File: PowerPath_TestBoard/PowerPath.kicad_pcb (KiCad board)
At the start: 2 copper layers, 105.4 x 62.9 mm, 102 parts, among them IC1 LM74502DDFR, J1 24V Test, J2 +24V_Ext, J3 12V Test, J4 5V Test, J5 3V Test, J6 +V_in_24V, J7 GND, J8 +Vin_5V, Q1 PSMN012-100YS, Q2 PSMN012-100YS, U1 MCP1826S_LDO, U2 LMR51635XDDCR, U3 LMR51635XDDCR

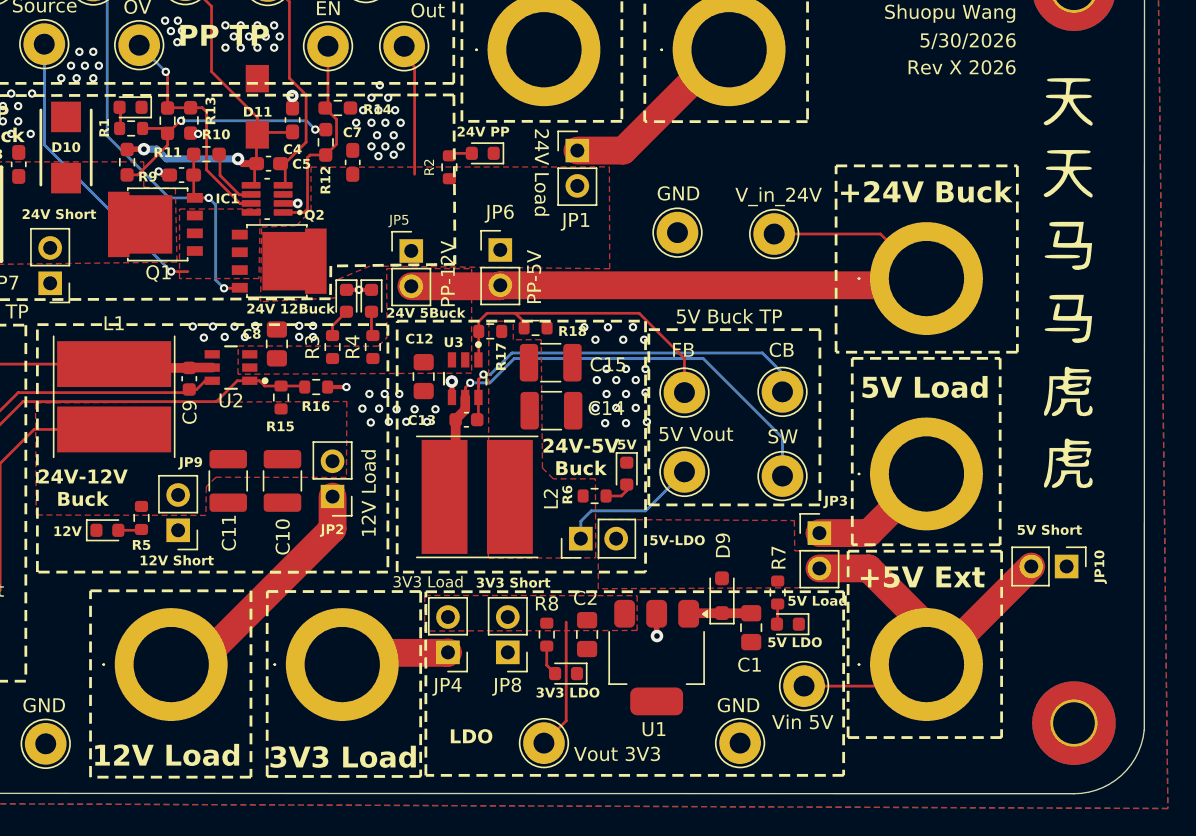
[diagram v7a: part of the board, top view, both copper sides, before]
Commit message: updated with new comments + new gen gebers
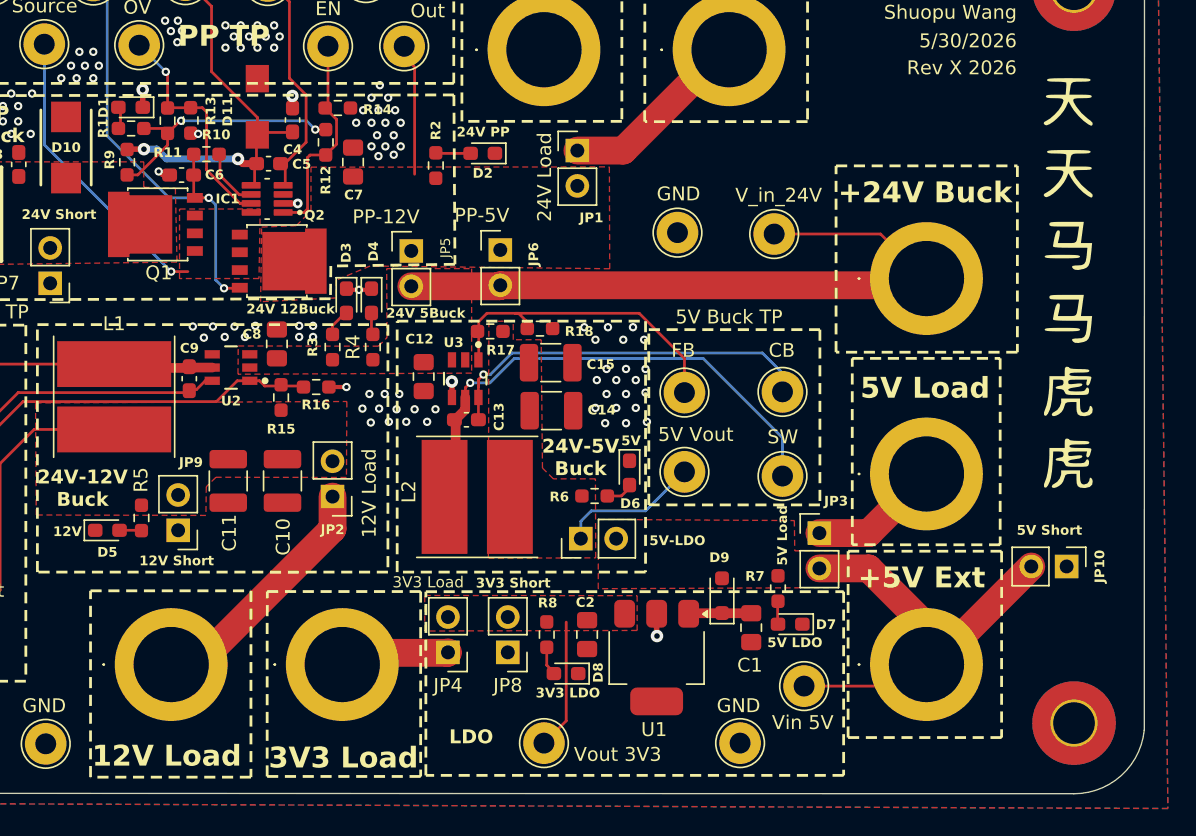
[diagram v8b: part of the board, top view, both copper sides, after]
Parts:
- C13, C9: footprint Capacitor_SMD:C_0603_1608Metric -> Capacitor_SMD:C_0603_1608Metric_Pad1.08x0.95mm_HandSolder
- C7: footprint Capacitor_SMD:C_0603_1608Metric_Pad1.08x0.95mm_HandSolder -> Capacitor_SMD:C_0805_2012Metric_Pad1.18x1.45mm_HandSolder
- D1, D2, D3, D4, D5, D6, D7, D8: footprint LED_SMD:LED_0603_1608Metric -> LED_SMD:LED_0603_1608Metric_Pad1.05x0.95mm_HandSolder
- R1, R15, R16, R17, R18, R2, R3, R4, R5, R6, R7, R8: footprint Resistor_SMD:R_0603_1608Metric -> Resistor_SMD:R_0603_1608Metric_Pad0.98x0.95mm_HandSolder
- moved R2 0.98 mm to (189.2, 79.9)
- moved R18 0.32 mm to (196.7, 91.6)
- moved R7 0.29 mm to (213.8, 110.3)
- moved D6 0.21 mm to (203.2, 102.0)
- moved D7 0.16 mm to (214.7, 112.8)
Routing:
- net GND: track 9.29 -> 10.6 mm, vias 102 -> 103
- net Net-(D2-A): track 1.68 -> 2.52 mm
